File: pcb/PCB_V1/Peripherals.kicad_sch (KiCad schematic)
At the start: 28 parts, among them J301 SHT4x / XH 2.50, J302 FLOAT / 3.5 mm, J401 Molex 104031-0811, U301 DS3231MZ+TRL

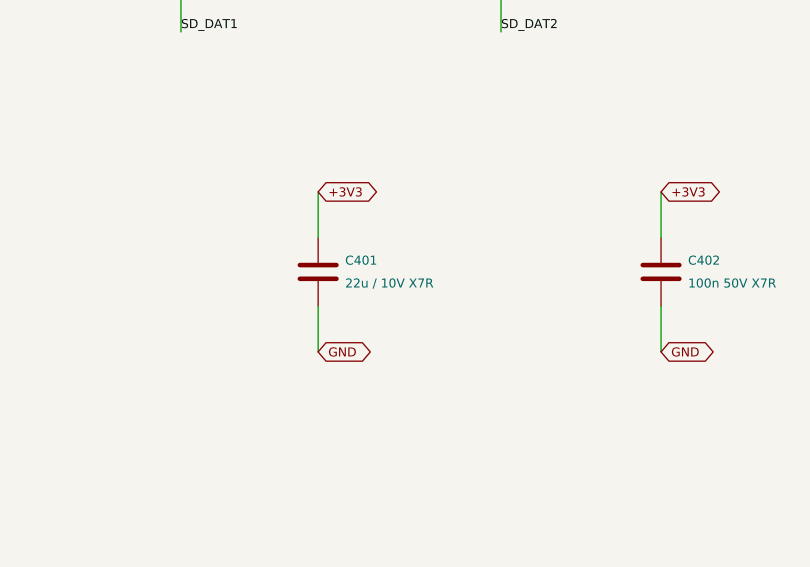
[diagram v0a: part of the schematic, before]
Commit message: pcb: revision 0.19 cost-down in the schematic, same footprints
Schematic and calculations only; PCB_V1.kicad_pcb is untouched on the
user's request. All substitutions keep footprints and nets.

- C716-C719, C726-C728: TDK C3225X7R2A106K250AC (X7R, published DC-bias
  curve 2.35 uF at 49 V) instead of Samsung CL32Y106KCV6PNE.
- C104/C105/C401: Samsung CL21A226MPQNNNE X5R; C521/C710/C715/C725/
  C905/C906: Taiyo Yuden UMK325AB7106KMHP.
- C602 shares CL21A106KAYNNNE with C201 (1.41 uF screen >= 1 uF);
  D601 shares SMBJ26CA with D901 (D_TVS symbol, 42.1 V clamp);
  R501/R511/R521 33R; F904 3 A shared with F721.
- analyze_led_power/analyze_power_path/verify_netlist updated; price and
  JLC snapshots v19; reports, sheet images and checks log v19.
- COST_DOWN.md: USD 37.50 per board (was 39.82), 65 purchase codes,
  rejected candidates and board status.

verify_board.py reports value differences for 17 parts until the board
is synced (footprints and nets already match); all other checks pass.

Co-Authored-By: Claude Opus 5.5 <noreply@anthropic.com>
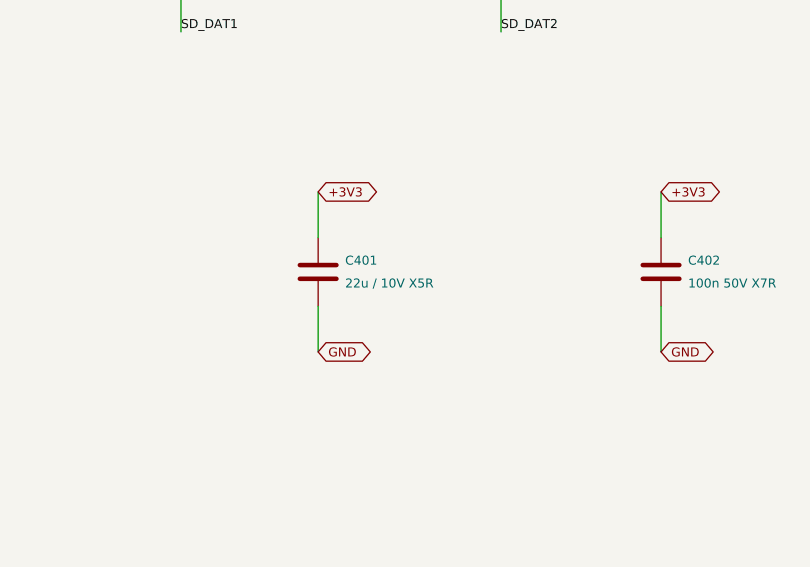
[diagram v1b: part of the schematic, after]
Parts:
- C401: value 22u / 10V X7R -> 22u / 10V X5R; LCSC (none) -> C29277; MPN (none) -> CL21A226MPQNNNE; Manufacturer (none) -> Samsung Electro-Mechanics
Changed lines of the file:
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@@
 			)
 		)
-		(property "Value" "22u / 10V X7R"
+		(property "Value" "22u / 10V X5R"
 			(at 284.94 177.8 0)
 			(show_name no)
@@
 			)
 		)
-		(property "Datasheet" ""
+		(property "Datasheet" "https://product.samsungsem.com/mlcc/CL21A226MPQNNN.do"
 			(at 281.94 176.53 0)
 			(hide yes)
@@
 			)
 		)
+		(property "Manufacturer" "Samsung Electro-Mechanics"
+			(at 281.94 176.53 0)
+			(effects
+				(font
+					(size 1 1)
+				)
+				(hide yes)
+			)
+		)
+		(property "LCSC" "C29277"
+			(at 281.94 176.53 0)
+			(effects
+				(font
+					(size 1 1)
+				)
+				(hide yes)
+			)
+		)
+		(property "MPN" "CL21A226MPQNNNE"
+			(at 281.94 176.53 0)
+			(effects
+				(font
+					(size 1 1)
+				)
+				(hide yes)
+			)
+		)

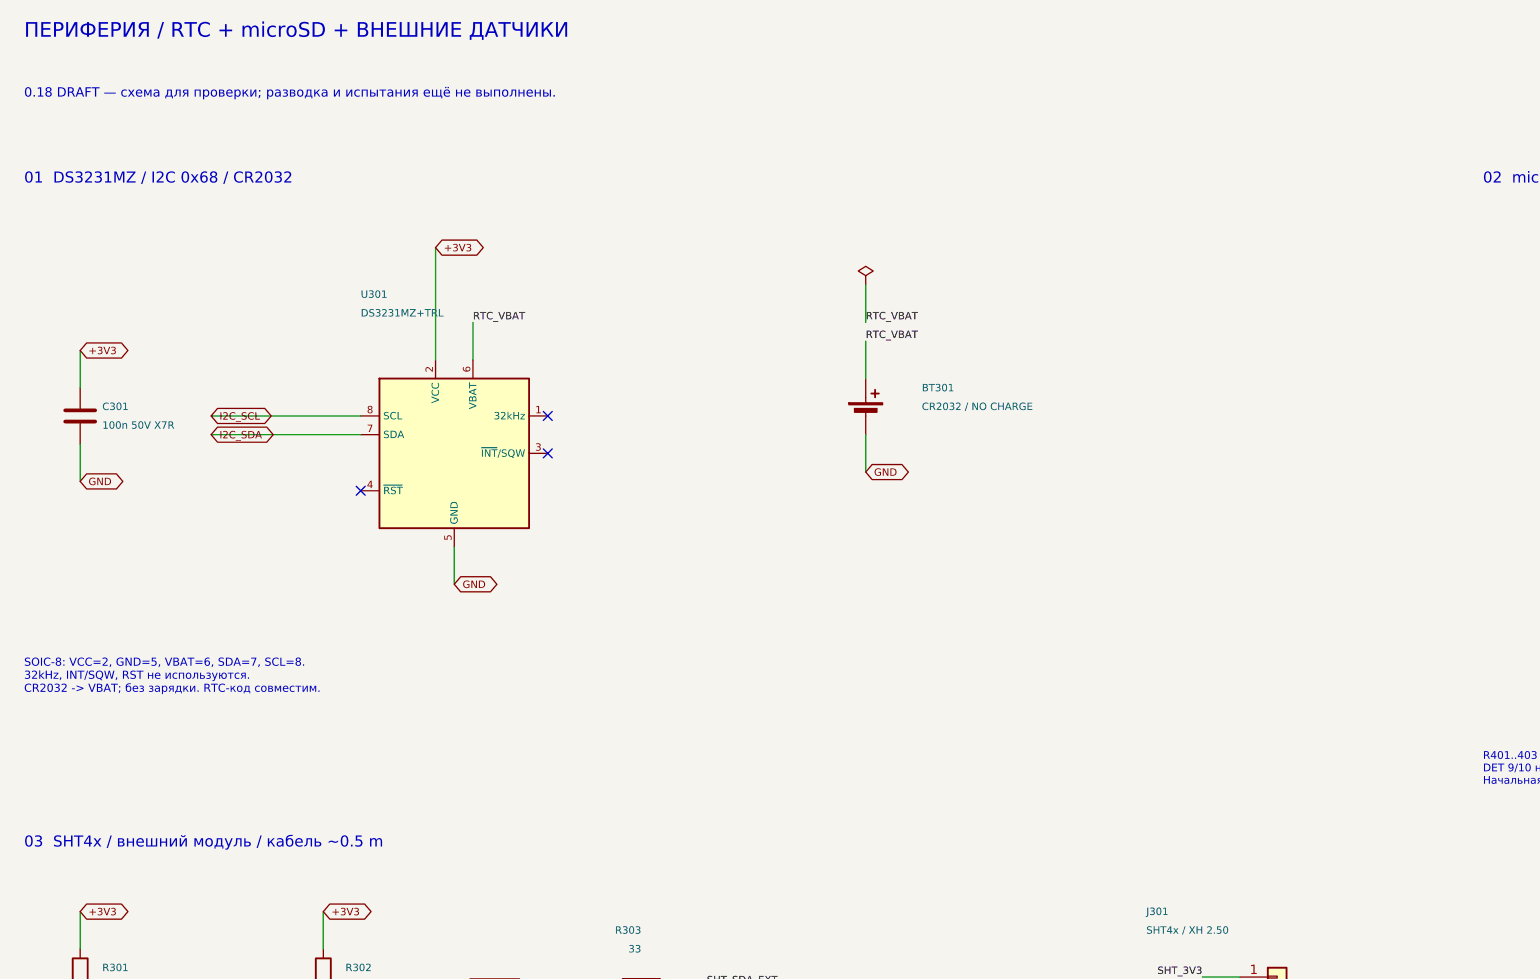
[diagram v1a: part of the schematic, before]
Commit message: pcb: revision 0.20 cost-down with new footprints and placement
- RTC: DS3231MZ replaced by NXP PCF8563T/5 with an Epson FC-135 crystal
  (CL 12.5 pF), C304 18 pF C0G on OSCI, BAT54C supply OR (D303) and R307
  1k from the CR2032.
- Boost switches Q711/Q721: AOS AOD66923 (DPAK) on a project footprint
  that keeps the S1/2/3 G4 D5 numbering; diodes D711/D721: Vishay SS5P10
  (TO-277A).
- L101 cjiang FXL0630-100-M and L902 PROD PSPMAA0604-220M-ANP on the
  KiCad FXL0630 land.
- LED switch areas and the RTC cluster re-placed (29 parts moved);
  ERC 0, DRC 0, 340 unrouted links.
- Checks, price/JLC snapshots v20, reports, placement images and docs
  updated: USD 31.62 per board (29.52 for five boards).

Co-Authored-By: Claude Opus 5.5 <noreply@anthropic.com>
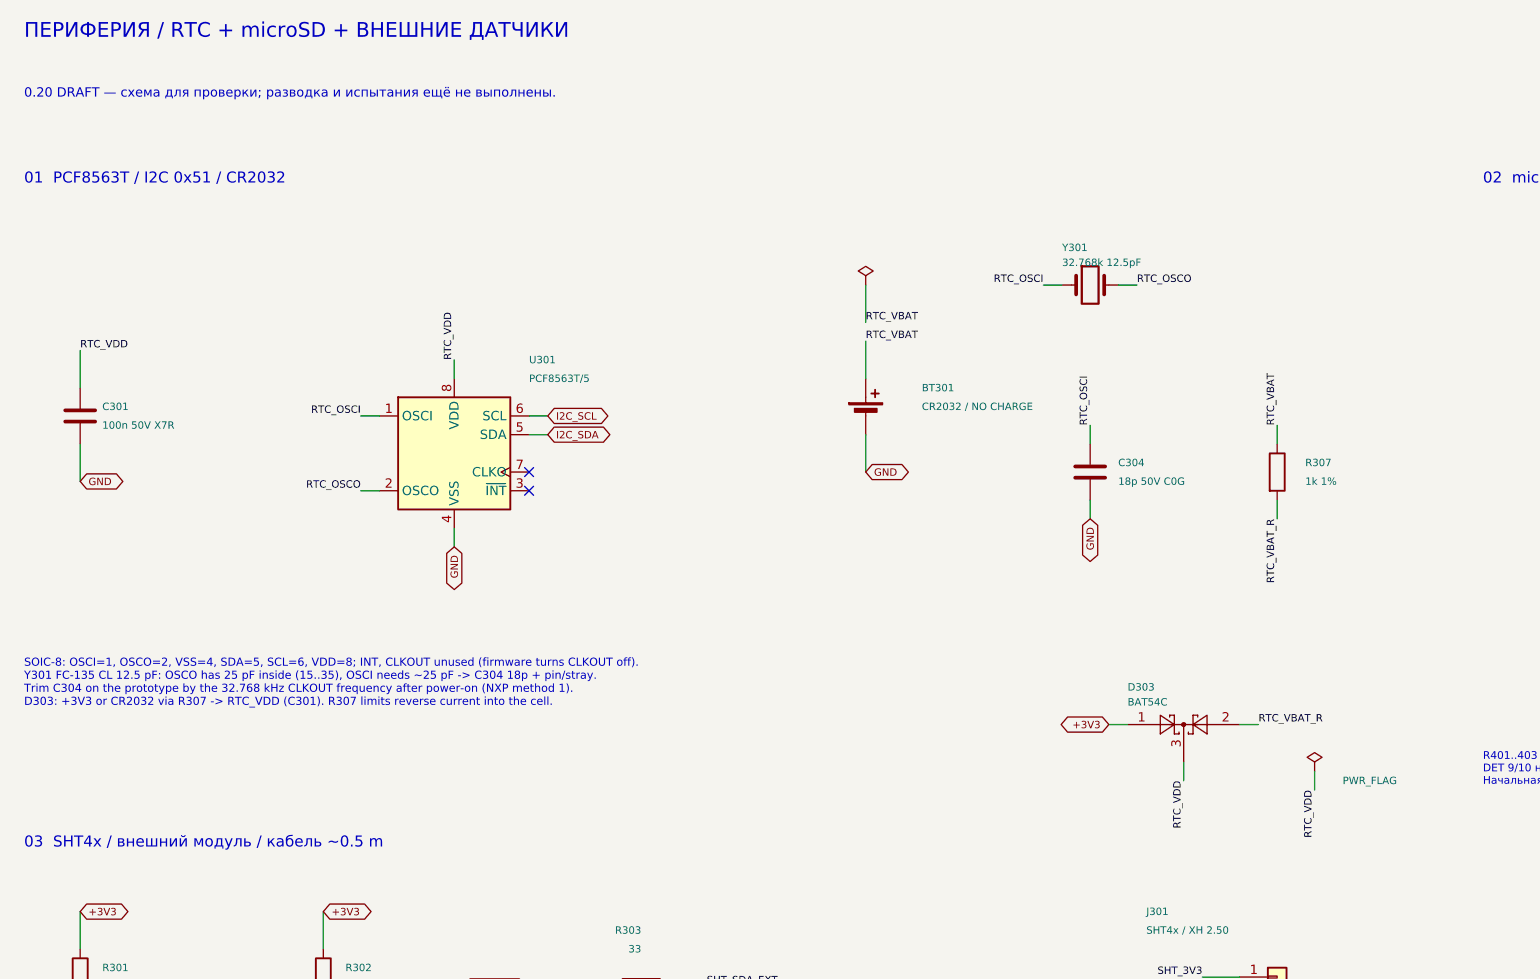
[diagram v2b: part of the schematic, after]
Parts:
- removed U301: DS3231MZ+TRL, Package_SO:SOIC-8_3.9x4.9mm_P1.27mm, symbol GrowBox:DS3231MZ
- added C304: 18p 50V C0G, Capacitor_SMD:C_0603_1608Metric, symbol Device:C
- added D303: BAT54C, Package_TO_SOT_SMD:SOT-23, symbol Diode:BAT54C
- added R307: 1k 1%, Resistor_SMD:R_0603_1608Metric, symbol Device:R
- added U301: PCF8563T/5, Package_SO:SOIC-8_3.9x4.9mm_P1.27mm, symbol Timer_RTC:PCF8563T
- added Y301: 32.768k 12.5pF, Crystal:Crystal_SMD_3215-2Pin_3.2x1.5mm, symbol Device:Crystal
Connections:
- net +3V3: now also D303.1; no longer C301.1
- net GND: now also C304.2, U301.4 (VSS)
- net I2C_SCL: now also U301.6 (SCL)
- net I2C_SDA: now also U301.5 (SDA)
- net RTC_VBAT: now also R307.1
- new net RTC_OSCI: C304.1, U301.1 (OSCI), Y301.1
- new net RTC_OSCO: U301.2 (OSCO), Y301.2
- new net RTC_VBAT_R: D303.2, R307.2
- new net RTC_VDD: C301.1, D303.3, U301.8 (VDD)
- no-connect marks 6 -> 5
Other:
- note added: "0.20 DRAFT — схема для проверки; разводка и испытания ещё не выполнены."
- note added: "01 PCF8563T / I2C 0x51 / CR2032"
- note added: "SOIC-8: OSCI=1, OSCO=2, VSS=4, SDA=5, SCL=6, VDD=8; INT, CLKOUT unused (firmware turns CLKOUT off). Y301 FC-135 CL 12.5 pF: OSCO has 25 pF inside (15..35), OSCI needs ~25 pF -> C304 18p + pin/stray. Trim C304 on the prototype by the 32.768 kHz CLKOUT frequency after power-on (NXP method 1). D303: +3V3 or CR2032 via R307 -> RTC_VDD (C301). R307 limits reverse current into the cell."
- note removed: "0.18 DRAFT — схема для проверки; разводка и испытания ещё не выполнены."
- note removed: "01 DS3231MZ / I2C 0x68 / CR2032"
- note removed: "SOIC-8: VCC=2, GND=5, VBAT=6, SDA=7, SCL=8. 32kHz, INT/SQW, RST не используются. CR2032 -> VBAT; без зарядки. RTC-код совместим."
